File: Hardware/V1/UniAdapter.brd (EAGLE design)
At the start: 30 x 21 mm, 24 parts, among them IC1 LD1117S33TR, IC2 SN65HVD232D, IC3 STM32F072CBT6, X1 CAN Bus, X2 CAN Bus

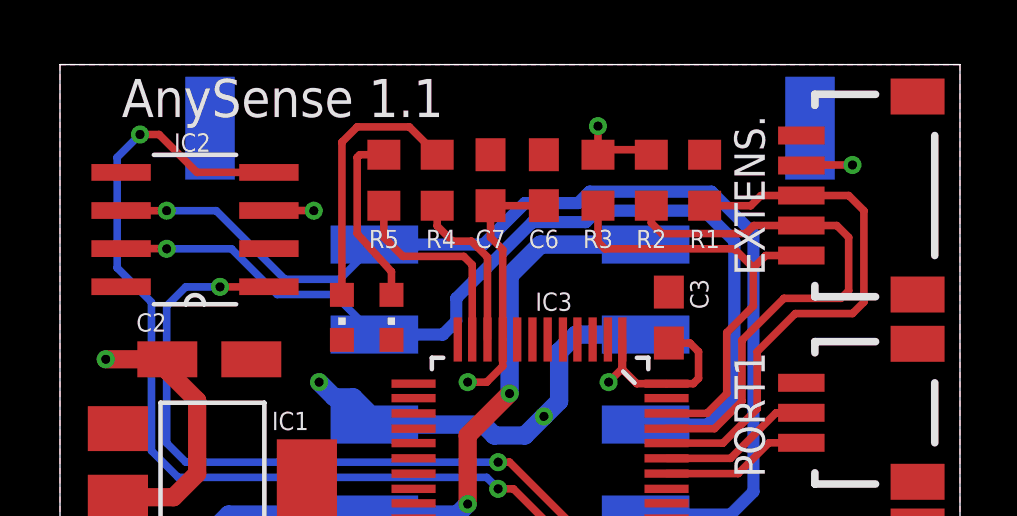
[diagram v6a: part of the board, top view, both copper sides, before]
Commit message: Order Codes changed, cream frame reduced, BOOT0 rerouted
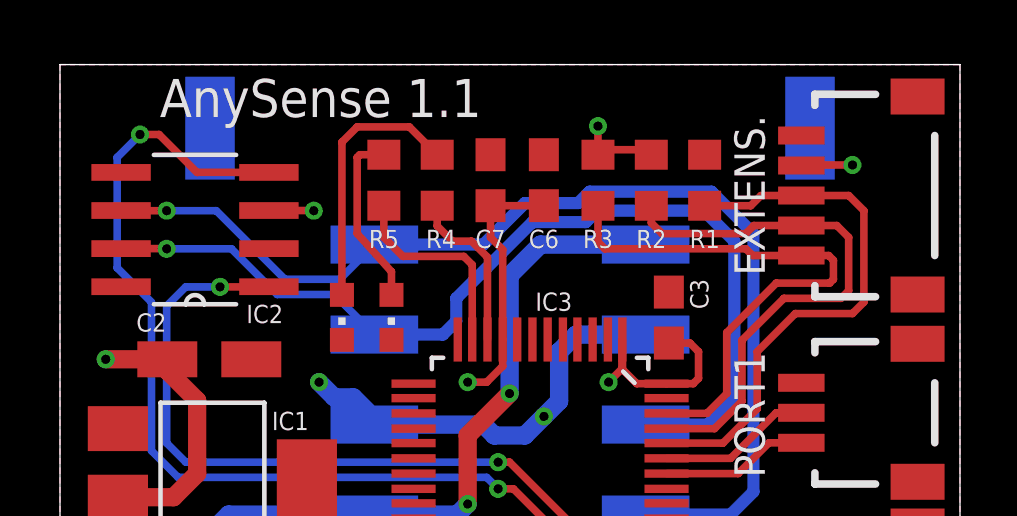
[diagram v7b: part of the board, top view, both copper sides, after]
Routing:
- net I2C1_SDA: track 15.4 -> 18.5 mm
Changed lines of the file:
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@@
 <wire x1="22.7097375" y1="1.53345" x2="37.66655" y2="1.53345" width="0.254" layer="49"/>
 <wire x1="37.66655" y1="1.53345" x2="37.7" y2="1.5" width="0.254" layer="49" curve="-90"/>
-<text x="2.0574" y="19.2504" size="1.27" layer="25" font="vector">AnySense 1.1</text>
+<text x="3.3274" y="19.2504" size="1.27" layer="25" font="vector">AnySense 1.1</text>
 </plain>
 <attributes>
@@
 <param name="psElongationOffset" value="100"/>
 <param name="mvStopFrame" value="0"/>
-<param name="mvCreamFrame" value="0.2"/>
+<param name="mvCreamFrame" value="0.1"/>
 <param name="mlMinStopFrame" value="0.075mm"/>
 <param name="mlMaxStopFrame" value="0.2mm"/>
@@
 <attribute name="NAME" x="21.4884" y="15.494" size="0.6096" layer="25" font="vector" rot="R180" align="bottom-center"/>
 <attribute name="VALUE" x="23.3934" y="16.51" size="1.27" layer="27" rot="R90"/>
-<attribute name="OC_FARNELL" value="2331740" x="21.4884" y="17.145" size="1.778" layer="27" rot="R90" display="off"/>
+<attribute name="OC_FARNELL" value="2059627" x="21.4884" y="17.145" size="1.778" layer="27" rot="R90" display="off"/>
 </element>
 <element name="IC2" library="texas" package="SOIC127P600X175-8N" value="SN65HVD232D" x="4.5" y="15.5" smashed="yes" rot="R180">
@@
 <attribute name="SUPPLIER" value="Texas Instruments" x="4.5" y="15.5" size="1.778" layer="27" rot="R180" display="off"/>
 <attribute name="OC_FARNELL" value="1103107" x="4.5" y="15.5" size="1.778" layer="27" rot="R180" display="off"/>
-<attribute name="NAME" x="3.798" y="18.0964" size="0.6096" layer="25" ratio="10" rot="SR0"/>
+<attribute name="NAME" x="6.211" y="12.3814" size="0.6096" layer="25" ratio="10" rot="SR0"/>
 <attribute name="VALUE" x="7.9544" y="21.215" size="2.0828" layer="27" ratio="10" rot="SR180"/>
 </element>
@@
 <attribute name="NAME" x="17.9324" y="15.494" size="0.6096" layer="25" align="top-center"/>
 <attribute name="VALUE" x="16.0274" y="17.78" size="1.27" layer="27" rot="R270"/>
-<attribute name="OC_FARNELL" value="2331730" x="17.9324" y="17.145" size="1.778" layer="27" rot="R270" display="off"/>
+<attribute name="OC_FARNELL" value="2059608" x="17.9324" y="17.145" size="1.778" layer="27" rot="R270" display="off"/>
 </element>
 <element name="R2" library="rcl" package="R0603" value="1.8K" x="19.7104" y="17.145" smashed="yes" rot="R270">
 <attribute name="NAME" x="19.7104" y="15.494" size="0.6096" layer="25" rot="R180" align="bottom-center"/>
 <attribute name="VALUE" x="17.8054" y="17.78" size="1.27" layer="27" rot="R270"/>
-<attribute name="OC_FARNELL" value="2331730" x="19.7104" y="17.145" size="1.778" layer="27" rot="R270" display="off"/>
+<attribute name="OC_FARNELL" value="2059608" x="19.7104" y="17.145" size="1.778" layer="27" rot="R270" display="off"/>
 </element>
 <element name="R4" library="rcl" package="R0603" value="68Ohm" x="12.573" y="17.145" smashed="yes" rot="R90">
 <attribute name="NAME" x="12.7" y="15.494" size="0.6096" layer="25" rot="R180" align="bottom-center"/>
 <attribute name="VALUE" x="14.478" y="16.51" size="1.27" layer="27" rot="R90"/>
-<attribute name="OC_FARNELL" value="2331710" x="12.573" y="17.145" size="1.778" layer="27" rot="R90" display="off"/>
+<attribute name="OC_FARNELL" value="2059570" x="12.573" y="17.145" size="1.778" layer="27" rot="R90" display="off"/>
 </element>
 <element name="R5" library="rcl" package="R0603" value="56Ohm" x="10.795" y="17.145" smashed="yes" rot="R90">
 <attribute name="NAME" x="10.795" y="15.494" size="0.6096" layer="25" rot="R180" align="bottom-center"/>
 <attribute name="VALUE" x="12.7" y="16.51" size="1.27" layer="27" rot="R90"/>
-<attribute name="OC_FARNELL" value="2331709" x="10.795" y="17.145" size="1.778" layer="27" rot="R90" display="off"/>
+<attribute name="OC_FARNELL" value="2059568" x="10.795" y="17.145" size="1.778" layer="27" rot="R90" display="off"/>
 </element>
 <element name="LD1" library="led" package="CHIPLED_0603" value="RED" x="9.398" y="12.573" smashed="yes" rot="R180">
@@
 <wire x1="21.5646" y1="9.3726" x2="22.225" y2="10.033" width="0.254" layer="1"/>
 <wire x1="22.225" y1="10.033" x2="22.225" y2="12.065" width="0.254" layer="1"/>
-<wire x1="22.225" y1="12.065" x2="23.114" y2="12.954" width="0.254" layer="1"/>
+<wire x1="22.225" y1="12.065" x2="23.876" y2="13.716" width="0.254" layer="1"/>
 <contactref element="EXTENS." pad="1"/>
-<wire x1="23.114" y1="12.954" x2="23.114" y2="14.224" width="0.254" layer="1"/>
-<wire x1="23.114" y1="14.224" x2="23.525" y2="14.635" width="0.254" layer="1"/>
-<wire x1="23.525" y1="14.635" x2="24.711" y2="14.635" width="0.254" layer="1"/>
 <contactref element="R3" pad="2"/>
-<wire x1="18.161" y1="14.859" x2="22.479" y2="14.859" width="0.254" layer="1"/>
-<wire x1="22.479" y1="14.859" x2="23.114" y2="14.224" width="0.254" layer="1"/>
+<wire x1="18.161" y1="14.859" x2="22.86" y2="14.859" width="0.254" layer="1"/>
 <wire x1="17.9324" y1="16.295" x2="17.9324" y2="15.0876" width="0.254" layer="1"/>
 <wire x1="17.9324" y1="15.0876" x2="18.161" y2="14.859" width="0.254" layer="1"/>
+<wire x1="23.876" y1="13.716" x2="25.654" y2="13.716" width="0.254" layer="1"/>
+<wire x1="25.654" y1="13.716" x2="25.781" y2="13.843" width="0.254" layer="1"/>
+<wire x1="25.781" y1="13.843" x2="25.781" y2="14.478" width="0.254" layer="1"/>
+<wire x1="25.781" y1="14.478" x2="25.624" y2="14.635" width="0.254" layer="1"/>
+<wire x1="25.624" y1="14.635" x2="24.711" y2="14.635" width="0.254" layer="1"/>
+<wire x1="24.711" y1="14.635" x2="23.084" y2="14.635" width="0.254" layer="1"/>
+<wire x1="23.084" y1="14.635" x2="22.86" y2="14.859" width="0.254" layer="1"/>
 </signal>
 <signal name="LD_RED">
